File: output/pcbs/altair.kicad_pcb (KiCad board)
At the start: 2 copper layers, 134.5 x 112 mm, 73 parts

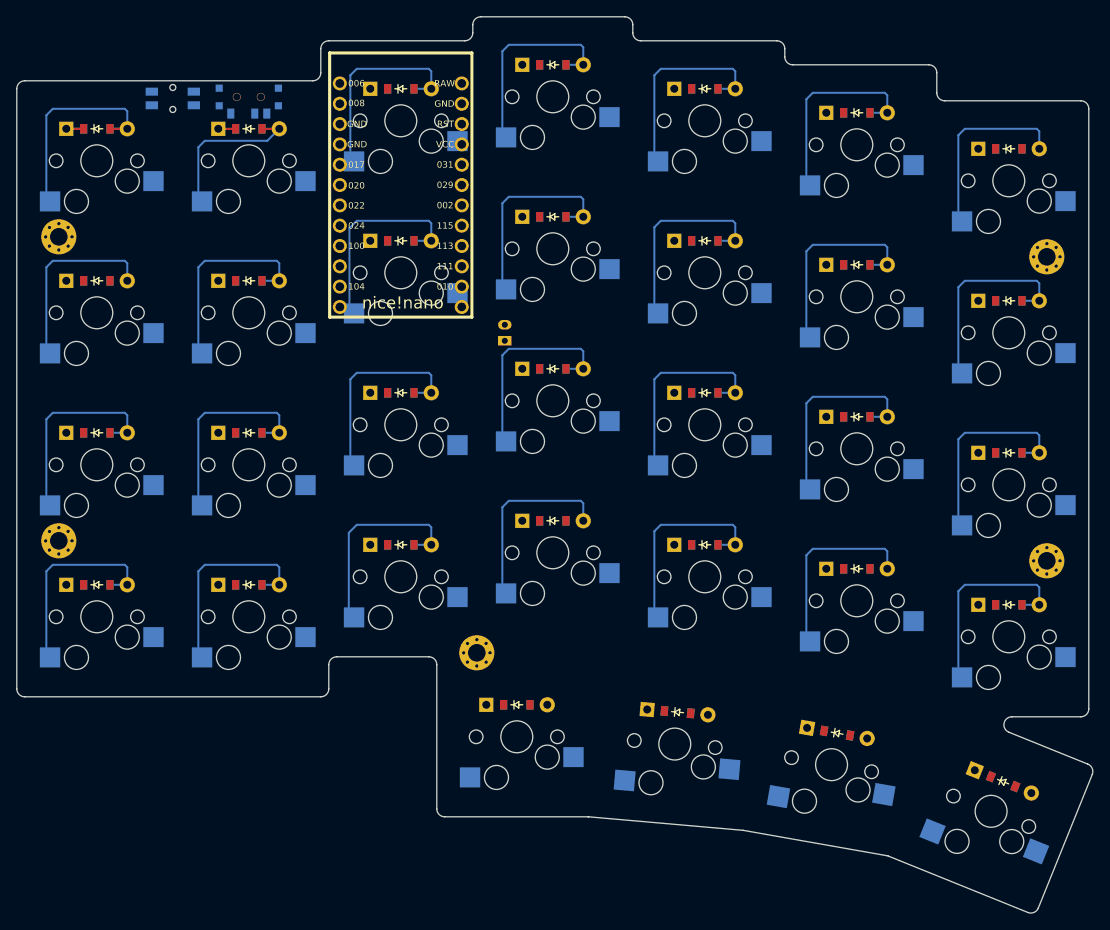
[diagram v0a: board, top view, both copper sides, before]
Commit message: Create column and row nets. Change position of MCU
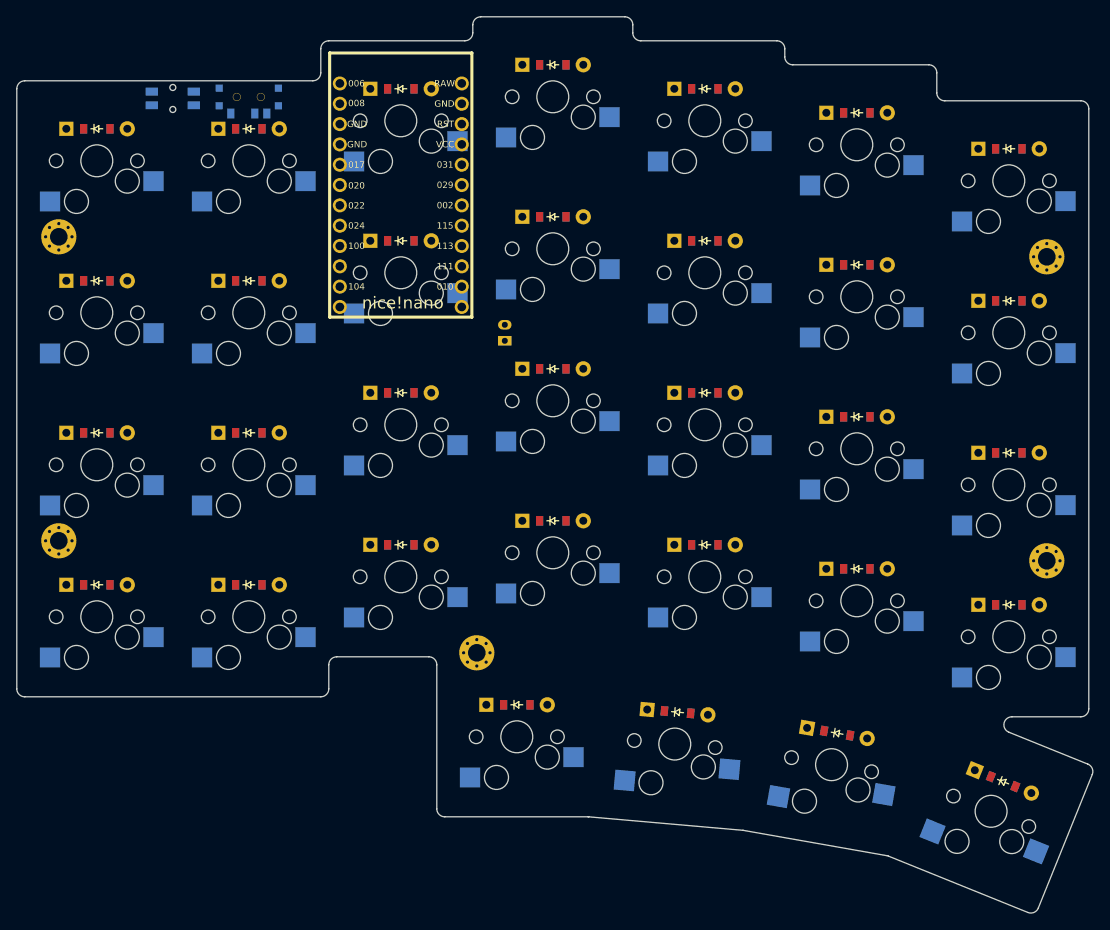
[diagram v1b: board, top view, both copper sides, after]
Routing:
- net left_num: track 28.1 -> 0.00 mm
- net ring_bottom: track 26.1 -> 0.00 mm
- net ring_top: track 26.0 -> 0.00 mm
- net right_bottom: track 25.9 -> 0.00 mm
- net ring_num: track 25.9 -> 0.00 mm
- net ring_home: track 25.9 -> 0.00 mm
- net right_top: track 25.9 -> 0.00 mm
- net right_home: track 25.9 -> 0.00 mm
- net middle_top: track 25.9 -> 0.00 mm
- net middle_home: track 25.9 -> 0.00 mm
- net inner_home: track 25.9 -> 0.00 mm
- net index_num: track 25.9 -> 0.00 mm
- net index_home: track 25.9 -> 0.00 mm
- net index_bottom: track 25.9 -> 0.00 mm
- net middle_num: track 25.9 -> 0.00 mm
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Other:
- net class Default added: clearance 0.2, trace_width 0.25, via_dia 0.8, via_drill 0.4

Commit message: create starting point for case
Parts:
- moved B1 41.9 mm to (92.2, 73.4), turned to 90 degrees
- moved _2 35.6 mm to (183.6, 49.4)
- moved T1 35.3 mm to (92.0, 57.7), turned to 90 degrees
- moved _1 35.3 mm to (130.4, 49.4)
- moved MCU1 29.2 mm to (109.0, 44.0), turned to 0 degrees
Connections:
- S1 pad 1: (no net) -> P031
- S10 pad 1: (no net) -> P002
- S11 pad 1: (no net) -> P002
- S12 pad 1: (no net) -> P002
- S13 pad 1: (no net) -> P115
- S14 pad 1: (no net) -> P115
- S15 pad 1: (no net) -> P115
- S16 pad 1: (no net) -> P115
- S17 pad 1: (no net) -> P017
- S18 pad 1: (no net) -> P017
- S19 pad 1: (no net) -> P017
- S2 pad 1: (no net) -> P031
- S20 pad 1: (no net) -> P017
- S21 pad 1: (no net) -> P020
- S22 pad 1: (no net) -> P020
- S23 pad 1: (no net) -> P020
- S24 pad 1: (no net) -> P020
- S25 pad 1: (no net) -> P022
- S26 pad 1: (no net) -> P022
- S27 pad 1: (no net) -> P022
- S28 pad 1: (no net) -> P022
- S29 pad 1: (no net) -> P115
- S3 pad 1: (no net) -> P031
- S30 pad 1: (no net) -> P017
- S31 pad 1: (no net) -> P020
- S32 pad 1: (no net) -> P022
- S4 pad 1: (no net) -> P031
- S5 pad 1: (no net) -> P029
- S6 pad 1: (no net) -> P029
- S7 pad 1: (no net) -> P029
- S8 pad 1: (no net) -> P029
- S9 pad 1: (no net) -> P002
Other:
- board size 134.5 x 112 mm -> 134.6 x 112.1 mm

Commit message: Change column and row nets
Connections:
- S1 pad 1: P031 -> P020
- S10 pad 1: P002 -> P111
- S11 pad 1: P002 -> P111
- S12 pad 1: P002 -> P111
- S13 pad 1: P115 -> P010
- S14 pad 1: P115 -> P010
- S15 pad 1: P115 -> P010
- S16 pad 1: P115 -> P010
- S17 pad 1: P017 -> P009
- S18 pad 1: P017 -> P009
- S19 pad 1: P017 -> P009
- S2 pad 1: P031 -> P020
- S20 pad 1: P017 -> P009
- S21 pad 1: P020 -> P029
- S22 pad 1: P020 -> P029
- S23 pad 1: P020 -> P029
- S24 pad 1: P020 -> P029
- S25 pad 1: P022 -> P031
- S26 pad 1: P022 -> P031
- S27 pad 1: P022 -> P031
- S28 pad 1: P022 -> P031
- S29 pad 1: P115 -> P010
- S3 pad 1: P031 -> P020
- S30 pad 1: P017 -> P009
- S31 pad 1: P020 -> P029
- S32 pad 1: P022 -> P031
- S4 pad 1: P031 -> P020
- S5 pad 1: P029 -> P106
- S6 pad 1: P029 -> P106
- S7 pad 1: P029 -> P106
- S8 pad 1: P029 -> P106
- S9 pad 1: P002 -> P111
